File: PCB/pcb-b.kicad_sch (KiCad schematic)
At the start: 22 parts, among them Q13 TPCA8120,L1Q, Q9 BC817, U1 L7805, U2 L7805, U3 L7805

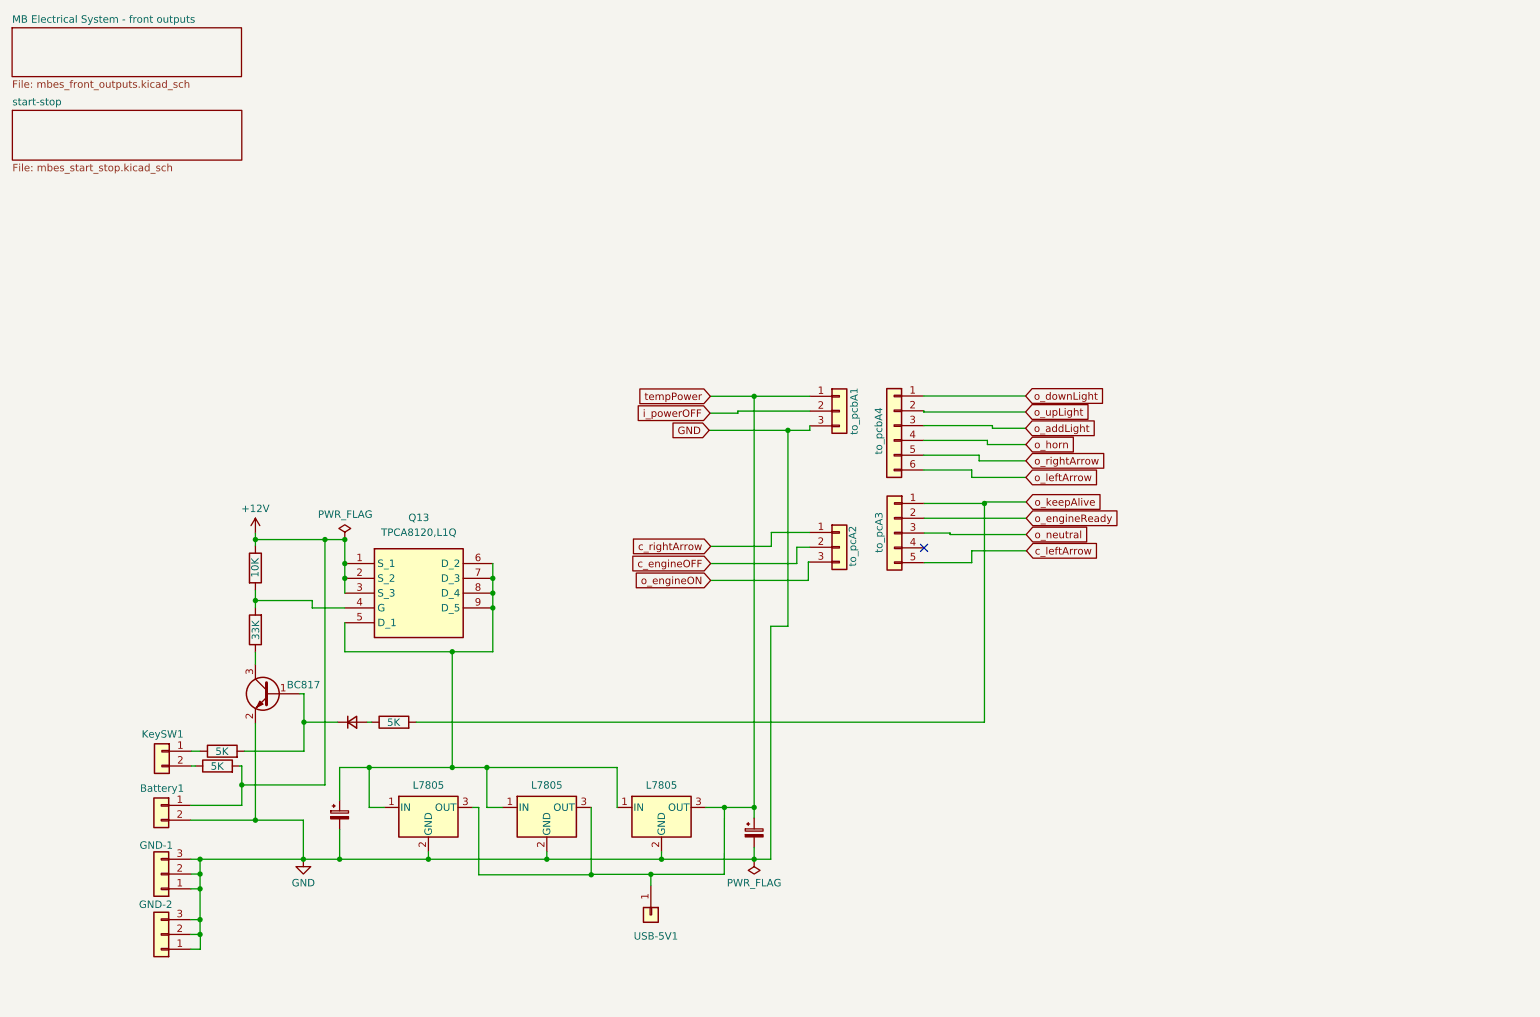
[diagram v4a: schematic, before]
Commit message: Pull-down resistor missing fixed
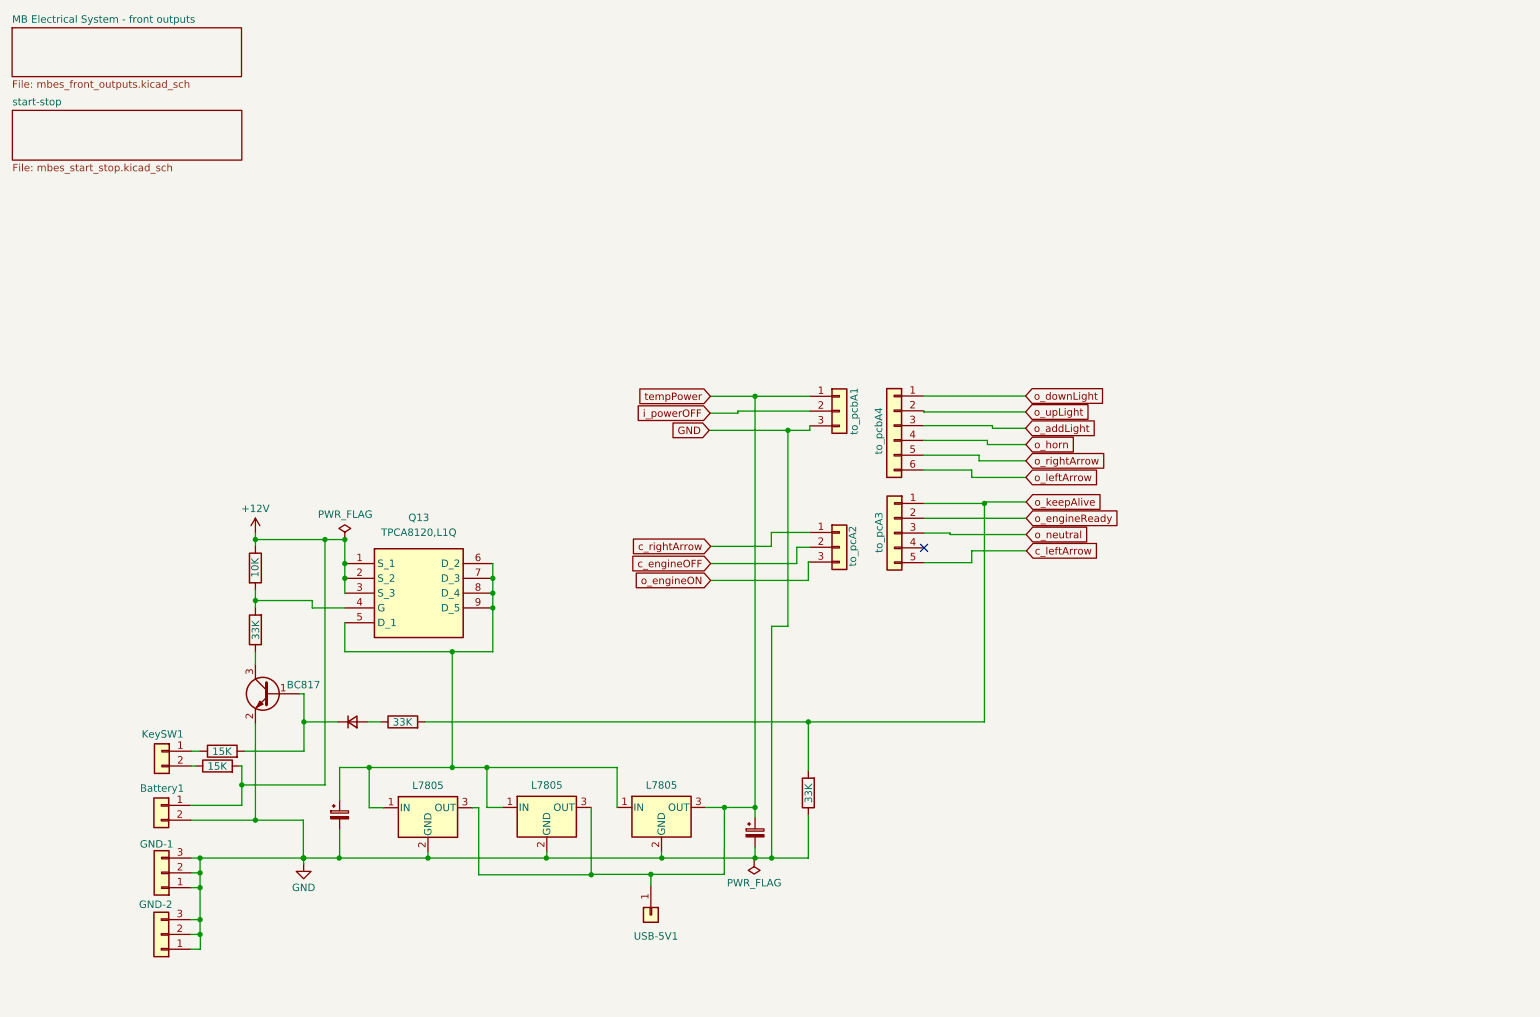
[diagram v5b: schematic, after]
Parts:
- added R6: 33K, Resistor_SMD:R_1206_3216Metric, symbol Device:R
- R1, R4: value 5K -> 15K
- R5: value 5K -> 33K
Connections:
- net GND: now also R6.1
- net o_keepAlive: now also R6.2

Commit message: USB Power Supply connector fixed
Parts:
- removed USB-5V1: Conn_01x01, Connector_Wire:SolderWire-1.5sqmm_1x01_D1.7mm_OD3.9mm, symbol Connector_Generic:Conn_01x01
- added USB-5V1: Conn_01x02, Connector_Wire:SolderWire-0.75sqmm_1x02_P7mm_D1.25mm_OD3.5mm, symbol Connector_Generic:Conn_01x02
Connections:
- net GND: now also USB-5V1.2 (Pin_2)
- net tempPower: now also USB-5V1.1 (Pin_1)
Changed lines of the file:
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@@
 	)
 	(junction
-		(at 123.0884 161.544)
-		(diameter 0)
-		(color 0 0 0 0)
-	)
-	(junction
 		(at 45.72 161.29)
 		(diameter 0)
@@
 	)
 	(junction
+		(at 72.644 158.75)
+		(diameter 0)
+		(color 0 0 0 0)
+	)
+	(junction
 		(at 70.5612 104.0892)
 		(diameter 0)
@@
 	)
 	(junction
+		(at 94.996 161.544)
+		(diameter 0)
+		(color 0 0 0 0)
+	)
+	(junction
 		(at 52.8828 146.2024)
 		(diameter 0)
@@
 	(wire
 		(pts
-			(xy 74.422 135.382) (xy 76.708 135.382)
+			(xy 94.996 180.086) (xy 94.996 161.544)
 		)
 		(stroke
@@
 	(wire
 		(pts
-			(xy 63.5 158.75) (xy 63.5 159.766)
+			(xy 74.422 135.382) (xy 76.708 135.382)
 		)
 		(stroke
@@
 	(wire
 		(pts
-			(xy 112.8268 161.544) (xy 112.8522 161.6202)
+			(xy 63.5 158.75) (xy 63.5 159.766)
 		)
 		(stroke
@@
 	(wire
 		(pts
-			(xy 84.836 157.734) (xy 84.836 158.75)
+			(xy 112.8268 161.544) (xy 112.8522 161.6202)
 		)
 		(stroke
@@
 	(wire
 		(pts
-			(xy 140.97 158.9532) (xy 140.8176 158.9532)
+			(xy 84.836 157.734) (xy 84.836 158.75)
 		)
 		(stroke
@@
 	(wire
 		(pts
-			(xy 69.596 158.75) (xy 84.836 158.75)
+			(xy 69.596 158.75) (xy 72.644 158.75)
 		)
 		(stroke
@@
 	(wire
 		(pts
-			(xy 112.8268 161.544) (xy 123.0884 161.544)
+			(xy 89.0016 143.2052) (xy 94.9452 143.2052)
 		)
 		(stroke
@@
 	(wire
 		(pts
-			(xy 89.0016 143.2052) (xy 94.9452 143.2052)
+			(xy 112.776 161.6202) (xy 112.8522 161.6202)
 		)
 		(stroke
@@
 	(wire
 		(pts
-			(xy 93.5482 150.114) (xy 92.456 150.114)
+			(xy 93.472 150.114) (xy 92.456 150.114)
 		)
 		(stroke
@@
 	(wire
 		(pts
-			(xy 93.5482 161.6202) (xy 93.5482 150.114)
+			(xy 93.472 161.544) (xy 93.472 150.114)
 		)
 		(stroke
@@
 	(wire
 		(pts
-			(xy 69.6722 143.2052) (xy 74.7522 143.2052)
+			(xy 44.196 182.626) (xy 72.644 182.626)
 		)
 		(stroke
@@
 	(wire
 		(pts
-			(xy 169.926 84.5312) (xy 181.7116 84.5312)
+			(xy 69.6722 143.2052) (xy 74.7522 143.2052)
 		)
 		(stroke
@@
 	(wire
 		(pts
-			(xy 74.7522 143.2052) (xy 89.0016 143.2052)
+			(xy 169.926 84.5312) (xy 181.7116 84.5312)
 		)
 		(stroke
@@
 	(wire
 		(pts
-			(xy 178.1556 92.1512) (xy 169.926 92.1512)
+			(xy 74.7522 143.2052) (xy 89.0016 143.2052)
 		)
 		(stroke
@@
 	(wire
 		(pts
-			(xy 64.9732 115.824) (xy 70.5612 115.824)
+			(xy 178.1556 92.1512) (xy 169.926 92.1512)
 		)
 		(stroke
@@
 	(wire
 		(pts
-			(xy 69.6722 158.496) (xy 69.6722 153.8732)
+			(xy 64.9732 115.824) (xy 70.5612 115.824)
 		)
 		(stroke
@@
 	(wire
 		(pts
-			(xy 133.2484 82.3976) (xy 138.0236 82.3976)
+			(xy 69.6722 158.496) (xy 69.6722 153.8732)
 		)
 		(stroke
@@
 	(wire
 		(pts
-			(xy 67.1576 104.0892) (xy 55.2196 104.0892)
+			(xy 133.2484 82.3976) (xy 138.0236 82.3976)
 		)
 		(stroke
@@
 	(wire
 		(pts
-			(xy 123.0884 161.544) (xy 123.0884 163.4236)
+			(xy 67.1576 104.0892) (xy 55.2196 104.0892)
 		)
 		(stroke
@@
 	(wire
 		(pts
-			(xy 93.5482 161.6202) (xy 112.8522 161.6202)
+			(xy 93.472 161.544) (xy 94.996 161.544)
 		)
 		(stroke
@@
 	(wire
 		(pts
-			(xy 140.97 158.75) (xy 140.97 158.9532)
+			(xy 140.97 158.75) (xy 140.97 159.512)
+		)
+		(stroke
+			(width 0)
+			(type default)
+		)
+	)
+	(wire
+		(pts
+			(xy 112.776 161.544) (xy 112.776 161.6202)
+		)
+		(stroke
+			(width 0)
+			(type default)
+		)
+	)
+	(wire
+		(pts
+			(xy 72.644 158.75) (xy 84.836 158.75)
+		)
+		(stroke
+			(width 0)
+			(type default)
+		)
+	)
+	(wire
+		(pts
+			(xy 72.644 182.626) (xy 72.644 158.75)
 		)
 		(stroke
@@
 	(wire
 		(pts
+			(xy 44.196 180.086) (xy 94.996 180.086)
+		)
+		(stroke
+			(width 0)
+			(type default)
+		)
+	)
+	(wire
+		(pts
+			(xy 94.996 161.544) (xy 112.776 161.544)
+		)
+		(stroke
+			(width 0)
+			(type default)
+		)
+	)
+	(wire
+		(pts
 			(xy 45.72 163.83) (xy 45.72 169.3164)
 		)
@@
 	(wire
 		(pts
-			(xy 123.0884 161.544) (xy 135.6868 161.544)
+			(xy 112.8268 161.544) (xy 135.6868 161.544)
 		)
 		(stroke
@@
 	(symbol
 		(lib_id "power:PWR_FLAG")
-		(at 140.8176 158.9532 180)
+		(at 140.97 159.512 180)
 		(unit 1)
 		(exclude_from_sim no)
@@
 		(dnp no)
 		(property "Reference" "#FLG0101"
-			(at 140.8176 160.8582 0)
+			(at 140.97 161.417 0)
 			(effects
 				(font
@@
 		)
 		(property "Value" "PWR_FLAG"
-			(at 140.8176 163.0172 0)
+			(at 140.97 163.576 0)
 			(effects
 				(font
@@
 		)
 		(property "Footprint" ""
-			(at 140.8176 158.9532 0)
+			(at 140.97 159.512 0)
 			(effects
 				(font
@@
 		)
 		(property "Datasheet" "~"
-			(at 140.8176 158.9532 0)
+			(at 140.97 159.512 0)
 			(effects
 				(font
@@
 		)
 		(property "Description" ""
-			(at 140.8176 158.9532 0)
+			(at 140.97 159.512 0)
 			(effects
 				(font
@@
 	)
 	(symbol
+		(lib_id "Connector_Generic:Conn_01x02")
+		(at 39.116 180.086 0)
+		(mirror y)
+		(unit 1)
+		(exclude_from_sim no)
+		(in_bom yes)
+		(on_board yes)
+		(dnp no)
+		(property "Reference" "USB-5V1"
+			(at 39.243 177.165 0)
+			(effects
+				(font
+					(size 1.27 1.27)
+				)
+			)
+		)
+		(property "Value" "Conn_01x02"
+			(at 39.116 176.53 0)
+			(effects
+				(font
+					(size 1.27 1.27)
+				)
+				(hide yes)
+			)
+		)
+		(property "Footprint" "Connector_Wire:SolderWire-0.75sqmm_1x02_P7mm_D1.25mm_OD3.5mm"
+			(at 39.116 180.086 0)
+			(effects
+				(font
+					(size 1.27 1.27)
+				)
+				(hide yes)
+			)
+		)
+		(property "Datasheet" "~"
+			(at 39.116 180.086 0)
+			(effects
+				(font
+					(size 1.27 1.27)
+				)
+				(hide yes)
+			)
+		)
+		(property "Description" ""
+			(at 39.116 180.086 0)
+			(effects
+				(font
+					(size 1.27 1.27)
+				)
+				(hide yes)
+			)
+		)
+		(pin "1"
+		)
+		(pin "2"
+		)
+		(instances
+			(project "pcb-b"
+				(path "/709d0967-afe5-49d3-92a5-d2bb94550bdb"
+					(reference "USB-5V1")
+					(unit 1)
+				)
+			)
+		)
+	)
+	(symbol
 		(lib_id "Regulator_Linear:L7805")
 		(at 124.9172 150.0632 0)
@@
 					(unit 1)
 				)
-			)
-		)
-	)
-	(symbol
-		(lib_id "Connector_Generic:Conn_01x01")
-		(at 123.0884 168.5036 270)
-		(unit 1)
-		(exclude_from_sim no)
-		(in_bom yes)
-		(on_board yes)
-		(dnp no)
-		(property "Reference" "USB-5V1"
-			(at 127.762 172.1612 90)
-			(effects
-				(font
-					(size 1.27 1.27)
-				)
-				(justify right)
-			)
-		)
-		(property "Value" "Conn_01x01"
-			(at 120.9548 167.2337 90)
-			(effects
-				(font
-					(size 1.27 1.27)
-				)
-				(justify right)
-				(hide yes)
-			)
-		)
-		(property "Footprint" "Connector_Wire:SolderWire-1.5sqmm_1x01_D1.7mm_OD3.9mm"
-			(at 123.0884 168.5036 0)
-			(effects
-				(font
-					(size 1.27 1.27)
-				)
-				(hide yes)
-			)
-		)
-		(property "Datasheet" "~"
-			(at 123.0884 168.5036 0)
-			(effects
-				(font
-					(size 1.27 1.27)
-				)
-				(hide yes)
-			)
-		)
-		(property "Description" ""
-			(at 123.0884 168.5036 0)
-			(effects
-				(font
-					(size 1.27 1.27)
-				)
-				(hide yes)
-			)
-		)
-		(pin "1"
-		)
-		(instances
-			(project "pcb-b"
-				(path "/709d0967-afe5-49d3-92a5-d2bb94550bdb"
-					(reference "USB-5V1")
-					(unit 1)
-				)

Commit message: Manual merging from the ATmega16__dualPCB branch
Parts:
- removed C1: C_Polarized_Small, Capacitor_THT:CP_Radial_D8.0mm_P2.50mm, symbol Device:C_Polarized_Small
- removed U1, U2, U3: L7805, Package_TO_SOT_THT:TO-220-3_Vertical, symbol Regulator_Linear:L7805
- removed USB-5V1: Conn_01x02, Connector_Wire:SolderWire-0.75sqmm_1x02_P7mm_D1.25mm_OD3.5mm, symbol Connector_Generic:Conn_01x02
- removed to_pcA2, to_pcbA1: Conn_01x03, Connector_PinSocket_2.54mm:PinSocket_1x03_P2.54mm_Vertical, symbol Connector_Generic:Conn_01x03
- removed to_pcA3: Conn_01x05, Connector_PinSocket_2.54mm:PinSocket_1x05_P2.54mm_Vertical, symbol Connector_Generic:Conn_01x05
- added D2, D3: D_Small, Diode_SMD:D_1210_3225Metric_Pad1.42x2.65mm_HandSolder, symbol Device:D_Small
- added K1: HK19F-DCxxV-SHC, Relay_THT:Relay_DPDT_Finder_30.22, symbol Relay:HK19F-DCxxV-SHC
- added Q3: BC817, Package_TO_SOT_SMD:SOT-23, symbol Transistor_BJT:BC817
- added RA15: 10K, Resistor_SMD:R_1206_3216Metric, symbol Device:R
- added RA8: 100K, Resistor_SMD:R_1206_3216Metric, symbol Device:R
- added extpwr1: Conn_01x02, Connector_PinHeader_2.54mm:PinHeader_1x02_P2.54mm_Vertical, symbol Connector_Generic:Conn_01x02
- added koso-1: Conn_01x03, Connector_PinHeader_2.54mm:PinHeader_1x03_P2.54mm_Vertical, symbol Connector_Generic:Conn_01x03
- added to_pcA2, to_pcbA1, to_pcbA3: Conn_01x04, Connector_PinSocket_2.54mm:PinSocket_1x04_P2.54mm_Vertical, symbol Connector_Generic:Conn_01x04
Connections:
- net +12V: now also koso-1.3 (Pin_3)
- net GND: now also K1.12, K1.22, Q3.2 (E), RA8.2, extpwr1.1 (Pin_1), koso-1.1 (Pin_1), to_pcbA1.2 (Pin_2)
- net c_engineOFF: now also K1.11, K1.21, to_pcA2.3 (Pin_3)
- net c_leftArrow: now also to_pcbA3.1 (Pin_1)
- net c_rightArrow: now also to_pcA2.2 (Pin_2)
- net i_powerOFF: now also D3.1 (K), to_pcbA1.3 (Pin_3)
- net o_engineON: now also RA15.1, to_pcA2.4 (Pin_4)
- net o_engineReady: now also to_pcbA3.3 (Pin_3)
- net o_keepAlive: now also to_pcbA3.4 (Pin_4)
- net tempPower: now also C9.1, Q13.5 (D_1), Q13.6 (D_2), Q13.7 (D_3), Q13.8 (D_4), Q13.9 (D_5), K1.A1, extpwr1.2 (Pin_2), koso-1.2 (Pin_2), to_pcbA1.4 (Pin_4)
- net o_horn renamed c_horn
- new net: D2.1 (K), Q3.1 (B), RA8.1
- new net: K1.A2, Q3.3 (C)
- new net: D2.2 (A), D3.2 (A), RA15.2
- new net c_neutral: to_pcbA3.2 (Pin_2)
- no-connect marks 1 -> 4
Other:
- removed sheet start-stop
- note added: "CDI"
- moved on the sheet: Q13, to_pcbA4

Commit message: Old files replaced.
They have been merged for error
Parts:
- removed D2, D3: D_Small, Diode_SMD:D_1210_3225Metric_Pad1.42x2.65mm_HandSolder, symbol Device:D_Small
- removed K1: HK19F-DCxxV-SHC, Relay_THT:Relay_DPDT_Finder_30.22, symbol Relay:HK19F-DCxxV-SHC
- removed Q3: BC817, Package_TO_SOT_SMD:SOT-23, symbol Transistor_BJT:BC817
- removed RA15: 10K, Resistor_SMD:R_1206_3216Metric, symbol Device:R
- removed RA8: 100K, Resistor_SMD:R_1206_3216Metric, symbol Device:R
- removed extpwr1: Conn_01x02, Connector_PinHeader_2.54mm:PinHeader_1x02_P2.54mm_Vertical, symbol Connector_Generic:Conn_01x02
- removed koso-1: Conn_01x03, Connector_PinHeader_2.54mm:PinHeader_1x03_P2.54mm_Vertical, symbol Connector_Generic:Conn_01x03
- removed to_pcA2, to_pcbA1, to_pcbA3: Conn_01x04, Connector_PinSocket_2.54mm:PinSocket_1x04_P2.54mm_Vertical, symbol Connector_Generic:Conn_01x04
- added C1: C_Polarized_Small, Capacitor_THT:CP_Radial_D8.0mm_P2.50mm, symbol Device:C_Polarized_Small
- added U1, U2, U3: L7805, Package_TO_SOT_THT:TO-220-3_Vertical, symbol Regulator_Linear:L7805
- added USB-5V1: Conn_01x02, Connector_Wire:SolderWire-0.75sqmm_1x02_P7mm_D1.25mm_OD3.5mm, symbol Connector_Generic:Conn_01x02
- added to_pcA2, to_pcbA1: Conn_01x03, Connector_PinSocket_2.54mm:PinSocket_1x03_P2.54mm_Vertical, symbol Connector_Generic:Conn_01x03
- added to_pcA3: Conn_01x05, Connector_PinSocket_2.54mm:PinSocket_1x05_P2.54mm_Vertical, symbol Connector_Generic:Conn_01x05
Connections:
- net GND: now also C1.2, U1.2 (GND), U2.2 (GND), U3.2 (GND), USB-5V1.2 (Pin_2), to_pcbA1.3 (Pin_3)
- net c_engineOFF: now also to_pcA2.2 (Pin_2)
- net c_leftArrow: now also to_pcA3.5 (Pin_5)
- net c_rightArrow: now also to_pcA2.1 (Pin_1)
- net i_powerOFF: now also to_pcbA1.2 (Pin_2)
- net o_engineON: now also to_pcA2.3 (Pin_3)
- net o_engineReady: now also to_pcA3.2 (Pin_2)
- net o_keepAlive: now also to_pcA3.1 (Pin_1)
- net tempPower: now also C1.1, U1.3 (OUT), U2.3 (OUT), U3.3 (OUT), USB-5V1.1 (Pin_1), to_pcbA1.1 (Pin_1); no longer C9.1, Q13.5 (D_1), Q13.6 (D_2), Q13.7 (D_3), Q13.8 (D_4), Q13.9 (D_5)
- net c_horn renamed o_horn
- new net: C9.1, Q13.5 (D_1), Q13.6 (D_2), Q13.7 (D_3), Q13.8 (D_4), Q13.9 (D_5), U1.1 (IN), U2.1 (IN), U3.1 (IN)
- new net o_neutral: to_pcA3.3 (Pin_3)
- no-connect marks 4 -> 1
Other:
- added sheet start-stop (mbes_start_stop.kicad_sch)
- note removed: "CDI"
- moved on the sheet: Q13, to_pcbA4
